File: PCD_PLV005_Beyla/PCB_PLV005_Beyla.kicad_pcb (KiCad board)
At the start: 2 copper layers, 50 x 50 mm, 43 parts, among them J1 PWR/QB, J2 Switch_In, Q1 DMG2302UK-7, Q2 DMP2123L-7, U2 74HC266, U3 74HC08, U4 74HC21, U5 74LVC1G17, U6 LTC6993xS6-1

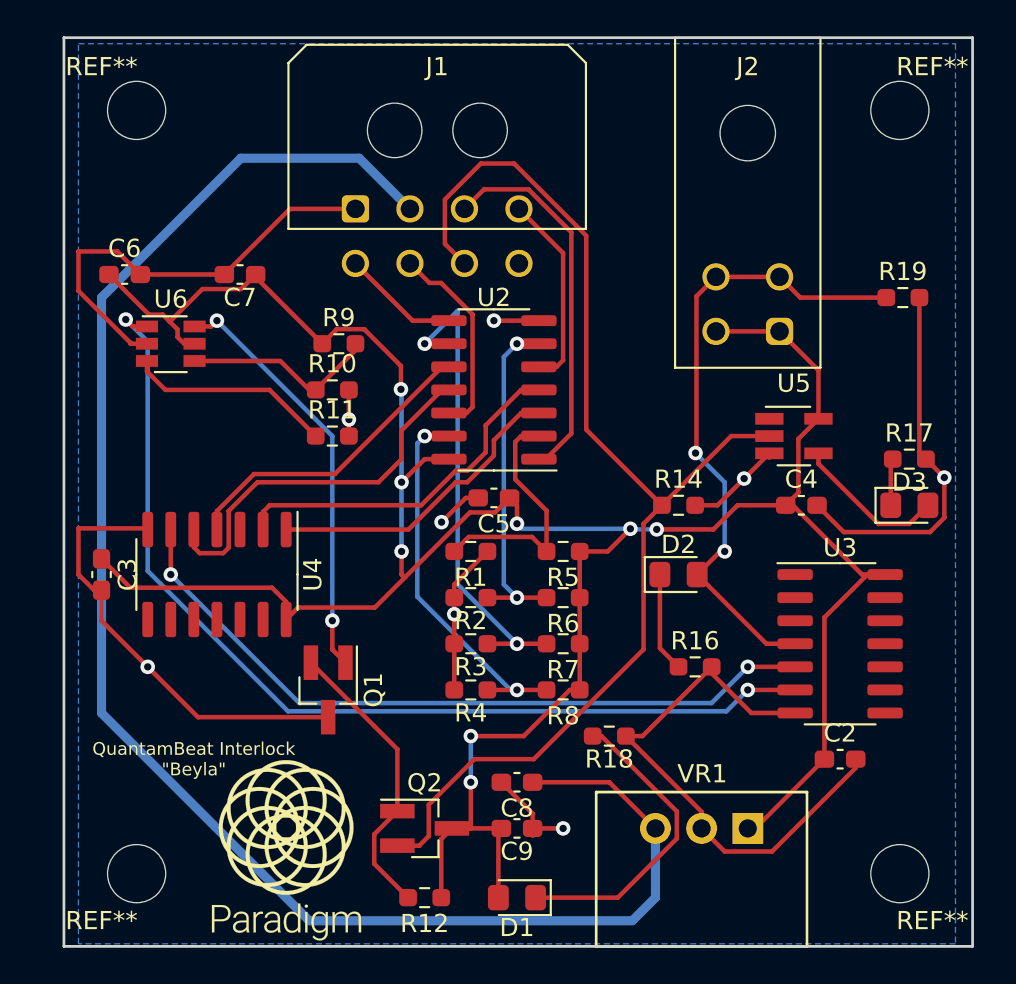
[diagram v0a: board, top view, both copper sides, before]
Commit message: Some Beyla Routing Changes
- Q1 and U8 overlap fixed
- Decoupling capacitors moved
- Transistor symbol fix in QB template schematic
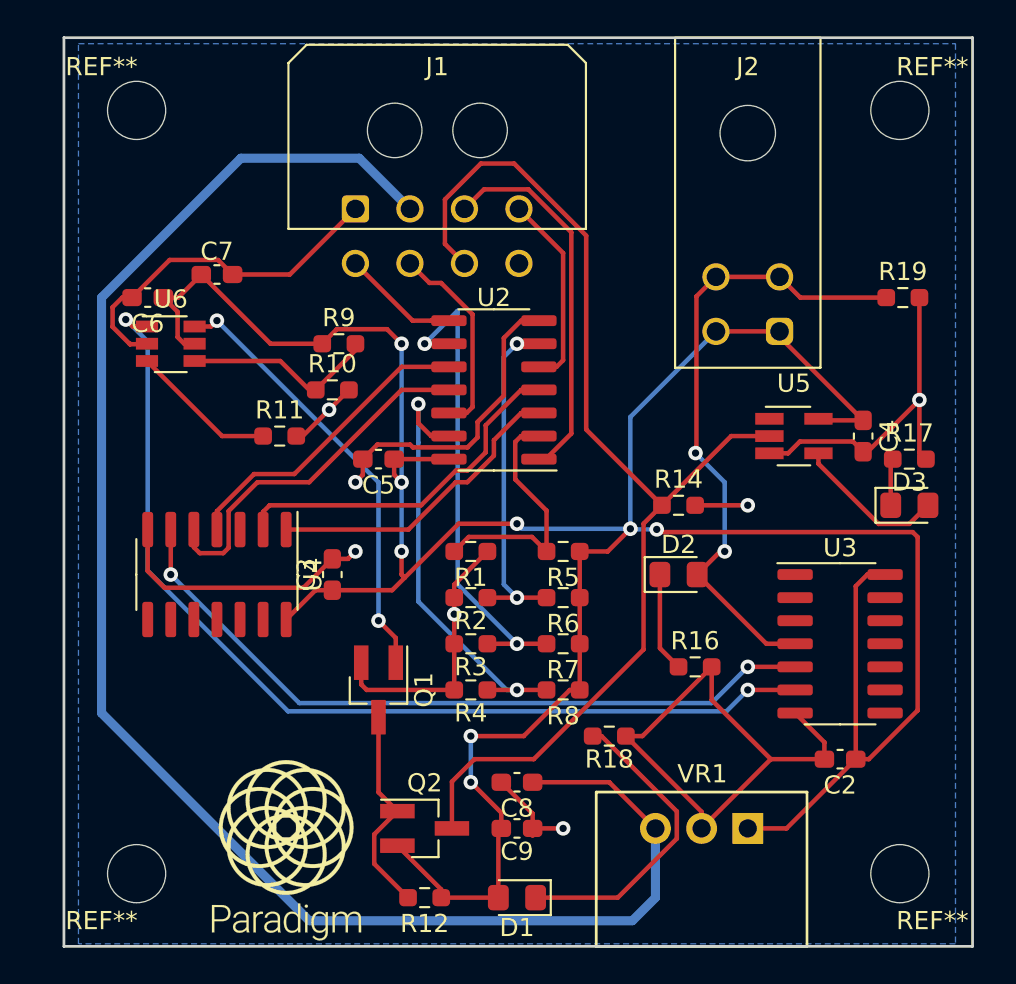
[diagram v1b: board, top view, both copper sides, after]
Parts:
- moved C3 12.7 mm to (64.8, 129.5), turned to 90 degrees
- moved C5 6.70 mm to (67.3, 123.2)
- moved C4 5.11 mm to (94.0, 121.9), turned to 270 degrees
- moved R11 2.90 mm to (61.9, 121.9)
- moved Q1 2.77 mm to (67.3, 135.9)
- moved C6 1.80 mm to (54.6, 114.3), turned to 180 degrees
- moved C7 1.27 mm to (58.4, 113.0), turned to 0 degrees
- turned C2 to 180 degrees
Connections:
- Q1 pad 2: Net-(Q1-Pad2) -> GND
- Q1 pad 3: GND -> Net-(Q1-Pad3)
- Q2 pad 1: Net-(Q1-Pad2) -> Net-(Q1-Pad3)
- Q2 pad 2: /AvionicsHeartbeatTemplate/HEARTBEAT -> +5V
- Q2 pad 3: +5V -> /AvionicsHeartbeatTemplate/HEARTBEAT
- R12 pad 2: Net-(Q1-Pad2) -> Net-(Q1-Pad3)
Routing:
- net Net-(Q1-Pad2): track 16.2 -> 0.00 mm
- net +5V: track 155.6 -> 167.7 mm
- net Net-(Q1-Pad3): track 0.00 -> 11.7 mm
- net Net-(R4-Pad2): track 21.2 -> 24.6 mm
- net Net-(R11-Pad1): track 11.3 -> 8.10 mm
- net /AvionicsHeartbeatTemplate/HEARTBEAT: track 65.6 -> 62.7 mm
- net GND: track 127.4 -> 129.7 mm, vias 8 -> 7
- net Net-(Q1-Pad1): track 23.1 -> 24.3 mm
- net Net-(U2-Pad11): track 21.0 -> 20.1 mm
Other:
- board text removed: "QuantamBeat Interlock "Beyla""

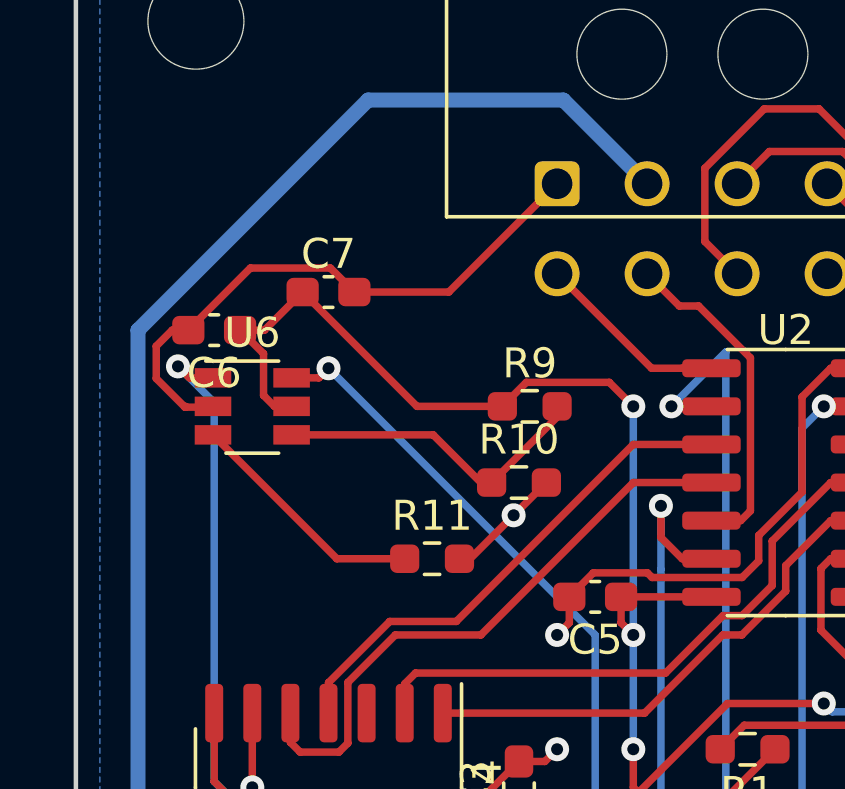
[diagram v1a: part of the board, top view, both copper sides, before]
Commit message: Beyla timer IC layout changes
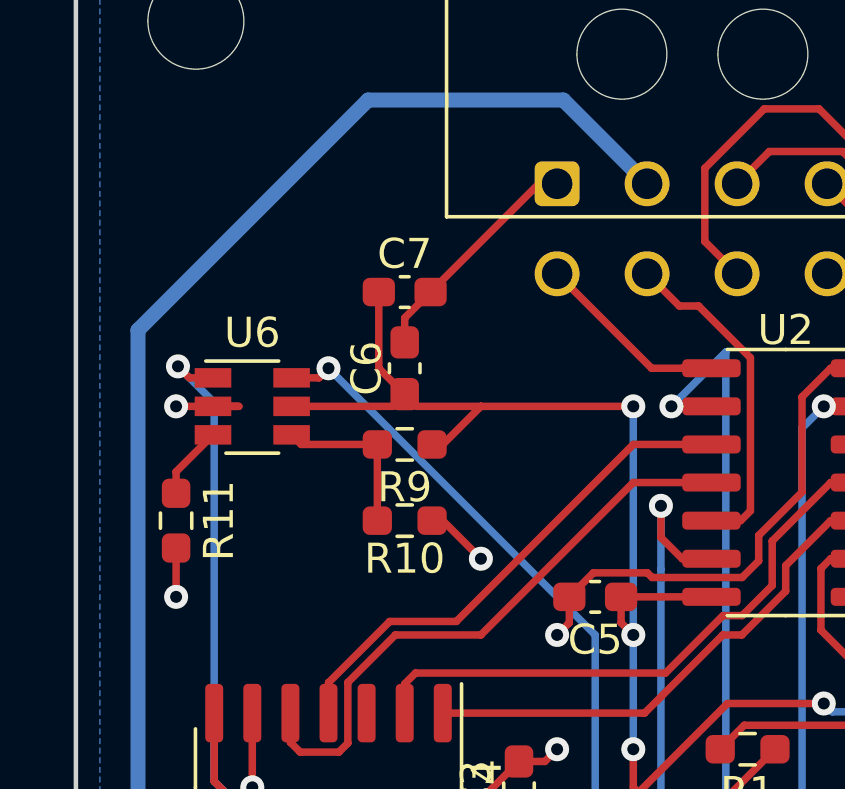
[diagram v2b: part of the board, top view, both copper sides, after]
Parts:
- moved R11 8.63 mm to (53.3, 120.7), turned to 270 degrees
- moved C6 6.48 mm to (61.0, 115.6), turned to 90 degrees
- moved R9 4.36 mm to (61.0, 118.1), turned to 180 degrees
- moved R10 4.02 mm to (61.0, 120.7)
- moved C7 2.54 mm to (61.0, 113.0)
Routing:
- net GND: track 129.7 -> 120.6 mm, vias 7 -> 9
- net Net-(R11-Pad1): track 8.10 -> 2.46 mm
- net Net-(R10-Pad1): track 10.8 -> 5.53 mm
- net +5V: track 167.7 -> 165.9 mm

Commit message: Beyla Layout Fixes
Fixed the problems with the first layout.
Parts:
- added REF**: Paradigm_Title_Block, BoringFootprints:Paradigm_Title_Block, F.Cu at (68.6, 147.3)
- G***: value (none) -> LOGO
- moved G*** 1.27 mm to (62.2, 143.5)
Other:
- board text added: "Paradigm Boring Beyla QuantumBeat Interlock"
